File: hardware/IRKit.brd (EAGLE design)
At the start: 54 x 56 mm, 75 parts, among them CN1 ZX62-B-5PA(11), IC1 ATMEGA32U4AU, IC2 TLV70233DBVT, IC3 LM386M-1, IC4 GS1011MXXS, SW1 EVQPUJ02K, T1 2SD1781KT146Q, T2 BSS138

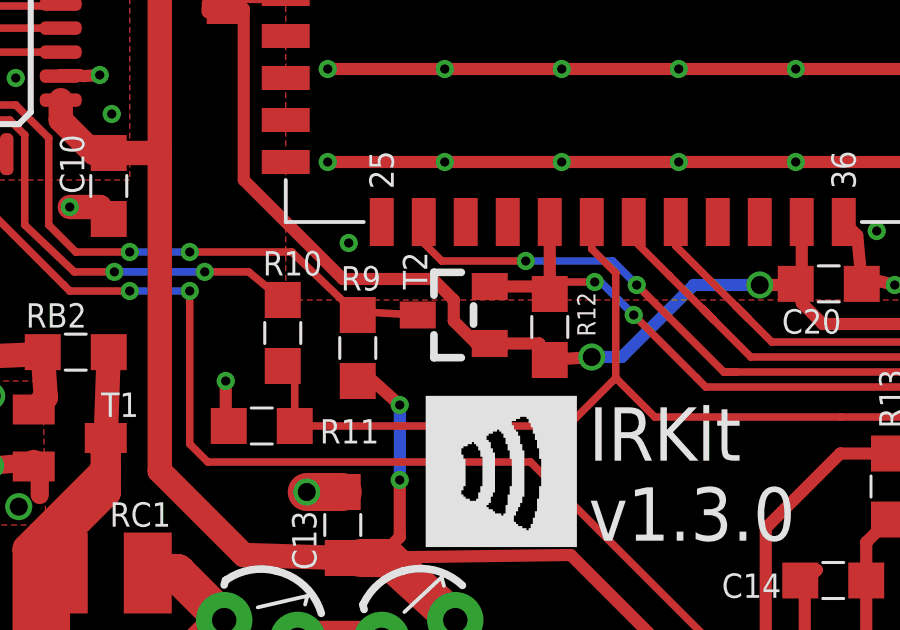
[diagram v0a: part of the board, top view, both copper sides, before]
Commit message: move bss138 to my.lbr
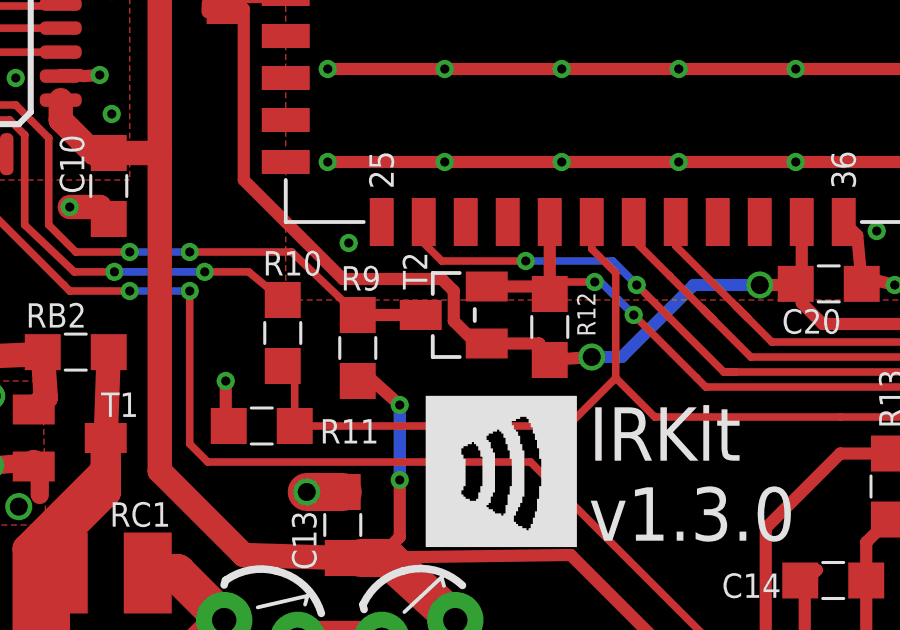
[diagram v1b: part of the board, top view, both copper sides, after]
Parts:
- T2: device m-pad-2.1:SOT23 -> my:SOT23
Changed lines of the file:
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@@
 <attribute name="VALUE" x="17.314" y="29.662" size="0.8128" layer="27" rot="R270"/>
 </element>
-<element name="T2" library="m-pad-2.1" package="SOT23" value="BSS138" x="30.8" y="15.5" smashed="yes" rot="R90">
+<element name="T2" library="my" package="SOT23" value="BSS138" x="30.8" y="15.5" smashed="yes" rot="R90">
 <attribute name="NAME" x="29.105" y="17.605" size="0.8128" layer="25" rot="R270"/>
 <attribute name="VALUE" x="33.975" y="13.595" size="0.8128" layer="27" rot="R90"/>
@@
 <wire x1="25.2" y1="39.5" x2="23.9" y2="38.2" width="0.4064" layer="1"/>
 <wire x1="23.5" y1="34.1" x2="21.9" y2="34.1" width="0.4064" layer="1"/>
-<wire x1="31.9" y1="14.8" x2="32" y2="14.55" width="0.4064" layer="1"/>
+<wire x1="31.9" y1="14.8" x2="31.9" y2="14.55" width="0.4064" layer="1"/>
 <wire x1="23.1625" y1="25.8" x2="23.4625" y2="26.2" width="0.4064" layer="1"/>
 <wire x1="23.4625" y1="26.2" x2="25.2" y2="26.2" width="0.6096" layer="1"/>
@@
 <wire x1="23.5" y1="34.1" x2="23.9" y2="34.5" width="0.4064" layer="1"/>
 <wire x1="23.9" y1="34.5" x2="23.9" y2="38.2" width="0.4064" layer="1"/>
-<wire x1="30.1" y1="16.7" x2="30.8" y2="16" width="0.4064" layer="1"/>
-<wire x1="30.8" y1="16" x2="30.8" y2="15.3" width="0.4064" layer="1"/>
 <wire x1="30.8" y1="15.3" x2="31.55" y2="14.55" width="0.4064" layer="1"/>
-<wire x1="31.55" y1="14.55" x2="32" y2="14.55" width="0.4064" layer="1"/>
-<wire x1="32" y1="14.55" x2="33.65" y2="14.55" width="0.4064" layer="1"/>
+<wire x1="31.55" y1="14.55" x2="31.9" y2="14.55" width="0.4064" layer="1"/>
+<wire x1="31.9" y1="14.55" x2="33.65" y2="14.55" width="0.4064" layer="1"/>
 <wire x1="33.65" y1="14.55" x2="34" y2="14" width="0.4064" layer="1"/>
 <wire x1="34" y1="14" x2="35.4" y2="14.1" width="0.4064" layer="1"/>
@@
 <wire x1="22.9" y1="40.5" x2="22.9" y2="40.7876" width="0.4064" layer="1"/>
 <wire x1="22.9" y1="40.7876" x2="21.8001" y2="41.8875" width="0.4064" layer="1"/>
+<wire x1="30.1" y1="16.7" x2="30.4" y2="16.7" width="0.4064" layer="1"/>
+<wire x1="30.4" y1="16.7" x2="30.8" y2="16.3" width="0.4064" layer="1"/>
+<wire x1="30.8" y1="16.3" x2="30.8" y2="15.3" width="0.4064" layer="1"/>
 </signal>
 <signal name="N$16">
@@
 <contactref element="CN3" pad="6"/>
 <via x="35.5" y="16.6" extent="1-16" drill="0.3048"/>
-<wire x1="32" y1="16.45" x2="33.75" y2="16.45" width="0.4064" layer="1"/>
+<wire x1="31.9" y1="16.45" x2="33.75" y2="16.45" width="0.4064" layer="1"/>
 <wire x1="33.75" y1="16.45" x2="34" y2="16.2" width="0.4064" layer="1"/>
 <wire x1="34" y1="16.2" x2="34" y2="18.6" width="0.4064" layer="1"/>
@@
 <wire x1="7.7375" y1="24.2625" x2="7.9375" y2="24.2625" width="0.254" layer="16"/>
 <wire x1="7.9375" y1="24.2625" x2="8.1375" y2="24.2625" width="0.254" layer="16"/>
-<wire x1="27.6" y1="15.5" x2="27.8" y2="15.6" width="0.254" layer="1"/>
-<wire x1="27.8" y1="15.6" x2="29.6" y2="15.5" width="0.254" layer="1"/>
 <wire x1="16.2" y1="22.5" x2="17.3" y2="21.4" width="0.254" layer="1"/>
 <wire x1="17.3" y1="21.4" x2="17.3" y2="18.5" width="0.254" layer="1"/>
@@
 <wire x1="9.9" y1="22.8" x2="10.2" y2="22.5" width="0.254" layer="1"/>
 <wire x1="10.2" y1="22.5" x2="16.2" y2="22.5" width="0.254" layer="1"/>
+<wire x1="27.6" y1="15.5" x2="29.7" y2="15.5" width="0.4064" layer="1"/>
 </signal>
 <signal name="A4/MIC">

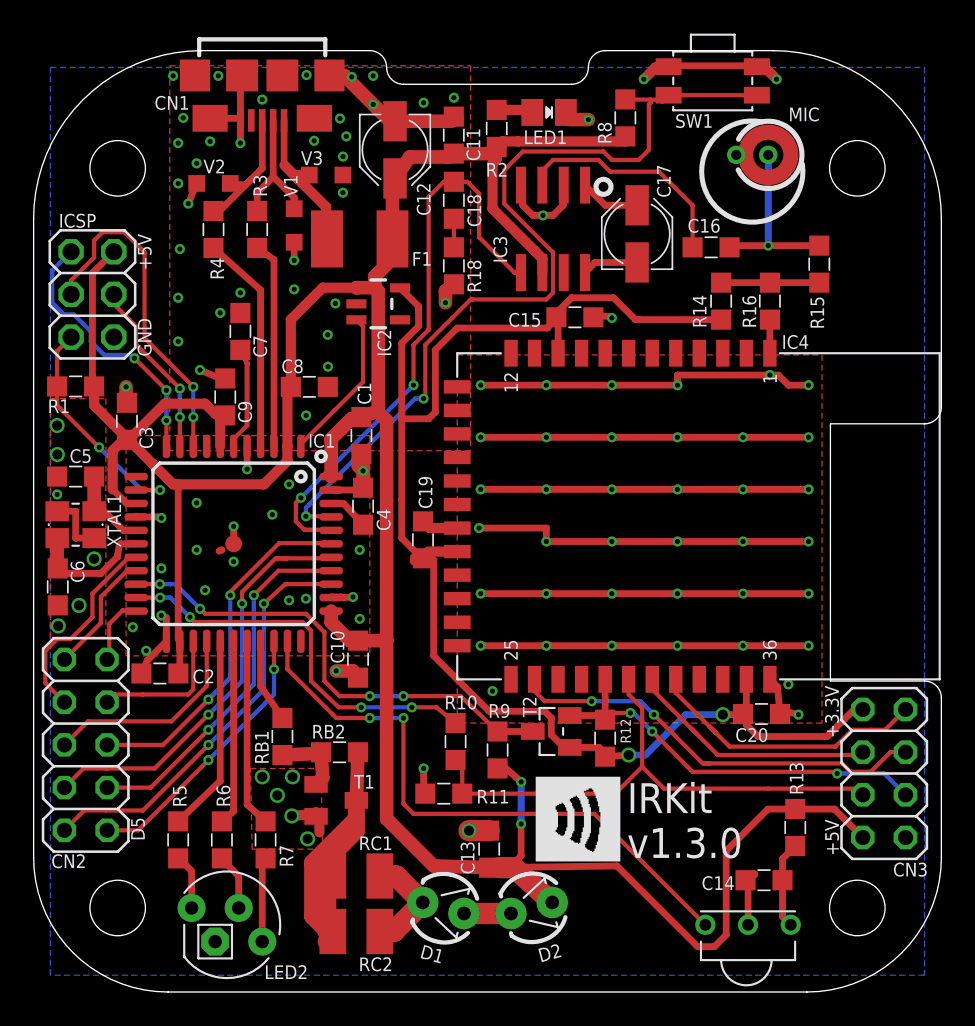
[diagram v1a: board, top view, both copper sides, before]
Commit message: pinheader's drill to 0.85 (to fit conthrough of switch-science)
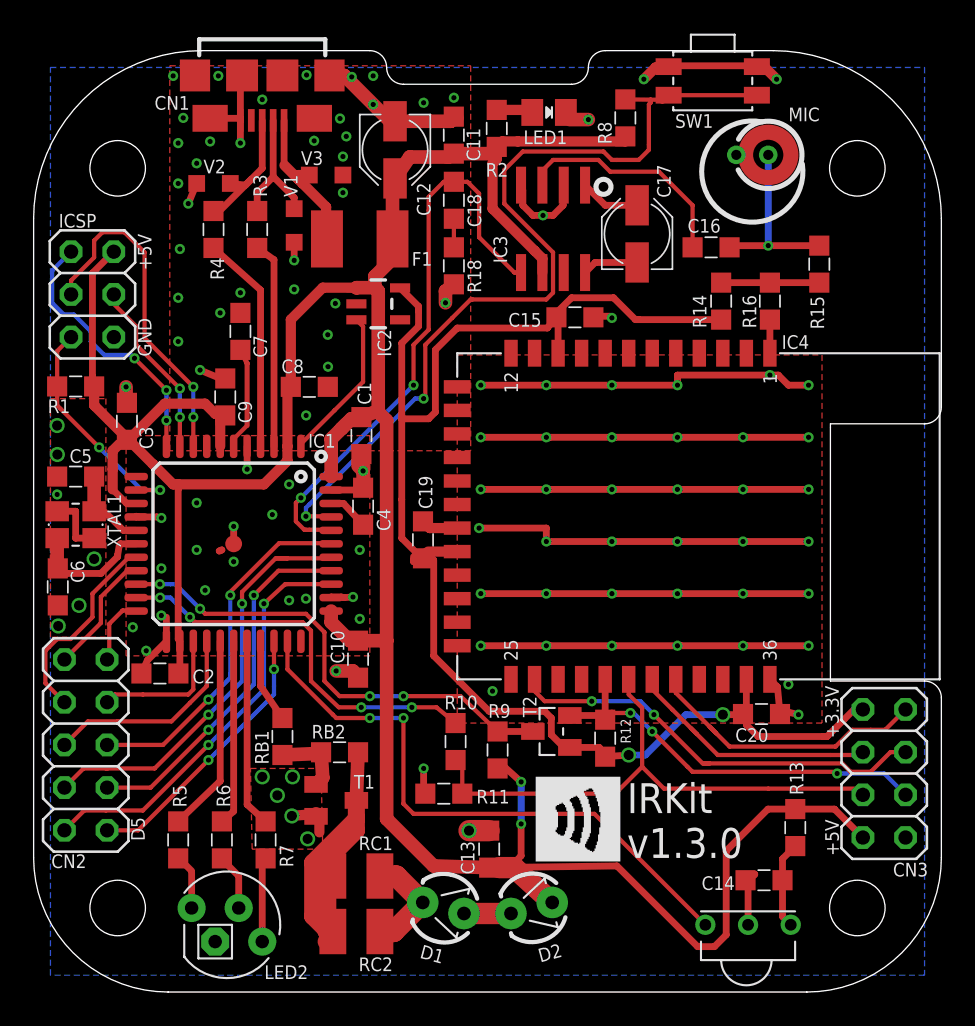
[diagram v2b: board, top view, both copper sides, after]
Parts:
- ICSP: device pinhead:2X03 -> my:2X03
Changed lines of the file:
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@@
 <element name="STANDOFF2" library="my" package="STAND-OFF" value="STAND-OFF" x="5" y="5" smashed="yes"/>
 <element name="STANDOFF4" library="my" package="STAND-OFF" value="STAND-OFF" x="5" y="49" smashed="yes"/>
-<element name="ICSP" library="pinhead" package="2X03" value="ICSP" x="3.5" y="41.5" smashed="yes" rot="R270">
+<element name="ICSP" library="my" package="2X03" value="ICSP" x="3.5" y="41.5" smashed="yes" rot="R270">
 <attribute name="NAME" x="1.49" y="45.475" size="0.8128" layer="25" ratio="10"/>
 <attribute name="VALUE" x="-0.945" y="45.31" size="0.8128" layer="27" rot="R270"/>

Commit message: replaced LED spacer to LK series package
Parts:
- SP1, SP2: value LA-6 -> LK-5; device my:LED-SPACER -> my:LED-SPACER-LK
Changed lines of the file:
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@@
 </element>
 <element name="U$1" library="logo" package="IRKIT-LOGO" value="" x="29.9" y="7.8"/>
-<element name="SP1" library="my" package="LED-SPACER" value="LA-6" x="29.625" y="5" rot="R195"/>
-<element name="SP2" library="my" package="LED-SPACER" value="LA-6" x="24.375" y="5" rot="R345"/>
+<element name="SP1" library="my" package="LED-SPACER-LK" value="LK-5" x="29.625" y="5" rot="R195"/>
+<element name="SP2" library="my" package="LED-SPACER-LK" value="LK-5" x="24.375" y="5" rot="R345"/>
 <element name="IC3" library="my" package="SO08" value="LM386M-1" x="30.9" y="45.4" smashed="yes" rot="R180">
 <attribute name="NAME" x="28.168" y="43.36" size="0.8128" layer="25" ratio="10" rot="R90"/>

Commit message: we use LM386M-1/NOPB variant
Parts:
- IC3: value LM386M-1 -> LM386M-1/NOPB
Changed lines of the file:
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@@
 <element name="SP1" library="my" package="LED-SPACER-LK" value="LK-5" x="29.625" y="5" rot="R195"/>
 <element name="SP2" library="my" package="LED-SPACER-LK" value="LK-5" x="24.375" y="5" rot="R345"/>
-<element name="IC3" library="my" package="SO08" value="LM386M-1" x="30.9" y="45.4" smashed="yes" rot="R180">
+<element name="IC3" library="my" package="SO08" value="LM386M-1/NOPB" x="30.9" y="45.4" smashed="yes" rot="R180">
 <attribute name="NAME" x="28.168" y="43.36" size="0.8128" layer="25" ratio="10" rot="R90"/>
 <attribute name="VALUE" x="27.598" y="47.94" size="1.27" layer="27" ratio="10" rot="R270"/>

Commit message: mic part no changed to KUB2823
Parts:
- MIC: value kus0323 -> KUB2823
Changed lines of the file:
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@@
 <attribute name="VALUE" x="27.598" y="47.94" size="1.27" layer="27" ratio="10" rot="R270"/>
 </element>
-<element name="MIC" library="my" package="MIC_SMD_4MM" value="kus0323" x="41.8" y="49.8" smashed="yes">
+<element name="MIC" library="my" package="MIC_SMD_4MM" value="KUB2823" x="41.8" y="49.8" smashed="yes">
 <attribute name="NAME" x="44.9" y="51.8" size="0.8128" layer="25"/>
 <attribute name="VALUE" x="43.7" y="47.6" size="0.8128" layer="27"/>

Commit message: make full color led darker
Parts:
- R5, R7: value 1k -> 3.3k
- R6: value 680 -> 2.2k
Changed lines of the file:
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@@
 <attribute name="VALUE" x="25.314" y="15.162" size="0.8128" layer="27" rot="R270"/>
 </element>
-<element name="R5" library="my" package="SMD2012" value="1k" x="8.6" y="9.05" smashed="yes" rot="R270">
+<element name="R5" library="my" package="SMD2012" value="3.3k" x="8.6" y="9.05" smashed="yes" rot="R270">
 <attribute name="NAME" x="9.0965" y="10.988" size="0.8128" layer="25" rot="R90"/>
 <attribute name="VALUE" x="6.314" y="9.812" size="0.8128" layer="27" rot="R270"/>
 </element>
-<element name="R6" library="my" package="SMD2012" value="680" x="11.2" y="9.05" smashed="yes" rot="R270">
+<element name="R6" library="my" package="SMD2012" value="2.2k" x="11.2" y="9.05" smashed="yes" rot="R270">
 <attribute name="NAME" x="11.6965" y="11.0005" size="0.8128" layer="25" rot="R90"/>
 <attribute name="VALUE" x="8.914" y="9.812" size="0.8128" layer="27" rot="R270"/>
@@
 <attribute name="NAME" x="13.725" y="0.775" size="0.8128" layer="21"/>
 </element>
-<element name="R7" library="my" package="SMD2012" value="1k" x="13.8" y="9.05" smashed="yes" rot="R270">
+<element name="R7" library="my" package="SMD2012" value="3.3k" x="13.8" y="9.05" smashed="yes" rot="R270">
 <attribute name="NAME" x="15.45" y="7.425" size="0.8128" layer="25" rot="R90"/>
 <attribute name="VALUE" x="11.9" y="10.05" size="1.016" layer="27" rot="R270"/>

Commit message: MIC part number changed to compatible one
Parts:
- MIC: value KUB2823 -> 254-ECM6044-RO
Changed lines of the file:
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@@
 <attribute name="VALUE" x="27.598" y="47.94" size="1.27" layer="27" ratio="10" rot="R270"/>
 </element>
-<element name="MIC" library="my" package="MIC_SMD_4MM" value="KUB2823" x="41.8" y="49.8" smashed="yes">
+<element name="MIC" library="my" package="MIC_SMD_4MM" value="254-ECM6044-RO" x="41.8" y="49.8" smashed="yes">
 <attribute name="NAME" x="44.9" y="51.8" size="0.8128" layer="25"/>
 <attribute name="VALUE" x="43.7" y="47.6" size="0.8128" layer="27"/>

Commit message: changed LED part no. to what I can buy in reel packaging
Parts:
- LED1: value OSG50805C1C -> PG1112H-TR
- R2: value 5.1k -> 2.2k
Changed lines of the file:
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@@
 </autorouter>
 <elements>
-<element name="R2" library="my" package="SMD2012" value="5.1k" x="27.55" y="51.375" smashed="yes" rot="R90">
+<element name="R2" library="my" package="SMD2012" value="2.2k" x="27.55" y="51.375" smashed="yes" rot="R90">
 <attribute name="NAME" x="26.893" y="48.501" size="0.8128" layer="25"/>
 <attribute name="VALUE" x="29.836" y="50.613" size="0.8128" layer="27" rot="R90"/>
@@
 <attribute name="VALUE" x="27.282" y="50.2115" size="0.8128" layer="27" rot="R90"/>
 </element>
-<element name="LED1" library="my" package="LED2012" value="OSG50805C1C" x="30.6625" y="52.325" smashed="yes">
+<element name="LED1" library="my" package="LED2012" value="PG1112H-TR" x="30.6625" y="52.325" smashed="yes">
 <attribute name="NAME" x="29.1405" y="50.441" size="0.8128" layer="25"/>
 <attribute name="VALUE" x="29.9005" y="50.039" size="0.8128" layer="27"/>
